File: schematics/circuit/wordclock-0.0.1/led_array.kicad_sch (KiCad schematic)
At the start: 67 parts, among them U2 MAX7219

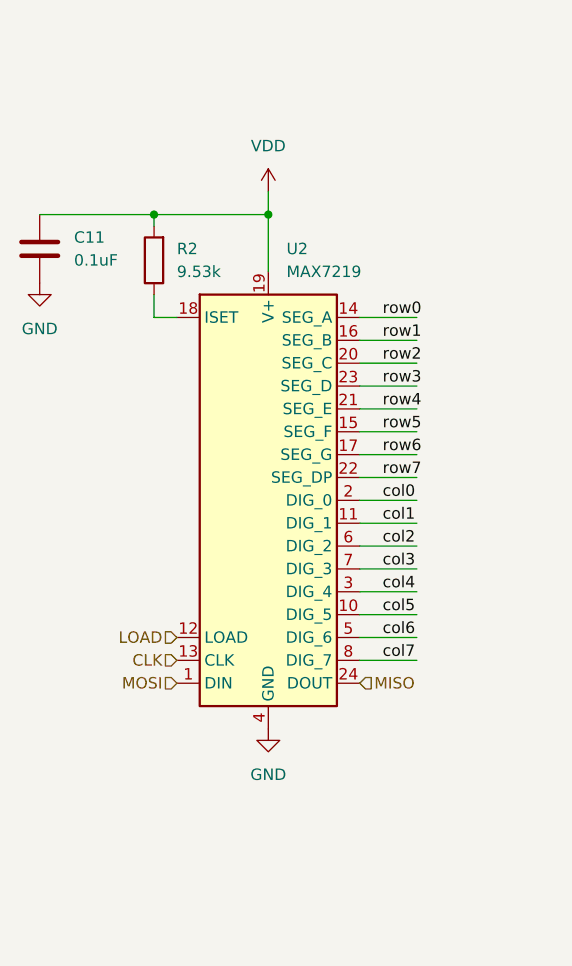
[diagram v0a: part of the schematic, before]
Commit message: Initial pcb layout
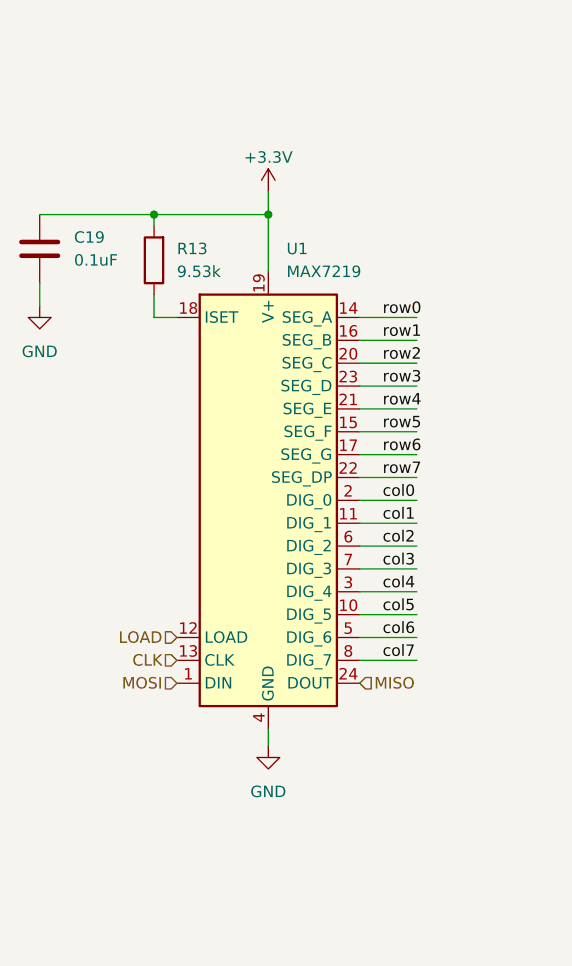
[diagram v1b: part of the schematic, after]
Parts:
- renumbered C11 to C19, R2 to R13, U2 to U1
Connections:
- net VDD renamed +3.3V
